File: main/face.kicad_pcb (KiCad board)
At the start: 2 copper layers, 100 x 100 mm, 114 parts

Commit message: added front face, moved around minute mark LEDs so they were spaced evenly and as close together as possible without interfering with USB
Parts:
- removed H1, H2, H3, H4: MountingHole, MountingHole:MountingHole_2.1mm
- added REF**: TestPoint_Pad_D4.0mm, TestPoint:TestPoint_Pad_D4.0mm, B.Cu at (7.81, 22.4)
- added REF**: TestPoint_Pad_D4.0mm, TestPoint:TestPoint_Pad_D4.0mm, B.Cu at (95.0, 5.00)
- added REF**: TestPoint_Pad_D4.0mm, TestPoint:TestPoint_Pad_D4.0mm, B.Cu at (95.0, 95.0)
- added REF**: TestPoint_Pad_D4.0mm, TestPoint:TestPoint_Pad_D4.0mm, B.Cu at (5.00, 95.0)
- added REF**: minute_hole, william_fab:minute_hole, F.Cu at (76.0, 92.6)
- added REF**: minute_hole, william_fab:minute_hole, F.Cu at (58.7, 92.6)
- added REF**: minute_hole, william_fab:minute_hole, F.Cu at (41.3, 92.6)
- added REF**: minute_hole, william_fab:minute_hole, F.Cu at (24.0, 92.6)
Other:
- board text added: "ABCDEFGHIJKL"
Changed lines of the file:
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@@
   (general
     (thickness 1.6)
-    (drawings 9)
+    (drawings 10)
     (tracks 0)
     (zones 0)
-    (modules 114)
+    (modules 118)
     (nets 1)
   )
@@
     (mod_text_size 0.6 0.6)
     (mod_text_width 0.13)
-    (pad_size 6 6)
-    (pad_drill 3)
+    (pad_size 4 4)
+    (pad_drill 0)
     (pad_to_mask_clearance 0.051)
     (solder_mask_min_width 0.25)
@@
     (uvia_drill 0.1)
   )
+  (module TestPoint:TestPoint_Pad_D4.0mm (layer B.Cu)
+    (at 7.814 22.414)
+    (descr "SMD pad as test Point, diameter 4.0mm")
+    (tags "test point SMD pad")
+    (attr virtual)
+    (fp_text reference REF** (at 0 2.898) (layer B.SilkS)
+      (effects (font (size 1 1) (thickness 0.15)) (justify mirror))
+    )
+    (fp_text value TestPoint_Pad_D4.0mm (at 0 -3.1) (layer B.Fab)
+      (effects (font (size 1 1) (thickness 0.15)) (justify mirror))
+    )
+    (fp_text user %R (at 0 2.9) (layer B.Fab)
+      (effects (font (size 1 1) (thickness 0.15)) (justify mirror))
+    )
+    (fp_circle (center 0 0) (end 2.5 0) (layer B.CrtYd) (width 0.05))
+    (fp_circle (center 0 0) (end 0 -2.25) (layer B.SilkS) (width 0.12))
+    (pad 1 smd circle (at 0 0) (size 4 4) (layers B.Cu B.Mask))
+  )
+  (module TestPoint:TestPoint_Pad_D4.0mm (layer B.Cu)
+    (at 95 5)
+    (descr "SMD pad as test Point, diameter 4.0mm")
+    (tags "test point SMD pad")
+    (attr virtual)
+    (fp_text reference REF** (at 0 2.898) (layer B.SilkS)
+      (effects (font (size 1 1) (thickness 0.15)) (justify mirror))
+    )
+    (fp_text value TestPoint_Pad_D4.0mm (at 0 -3.1) (layer B.Fab)
+      (effects (font (size 1 1) (thickness 0.15)) (justify mirror))
+    )
+    (fp_circle (center 0 0) (end 0 -2.25) (layer B.SilkS) (width 0.12))
+    (fp_circle (center 0 0) (end 2.5 0) (layer B.CrtYd) (width 0.05))
+    (fp_text user %R (at 0 2.9) (layer B.Fab)
+      (effects (font (size 1 1) (thickness 0.15)) (justify mirror))
+    )
+    (pad 1 smd circle (at 0 0) (size 4 4) (layers B.Cu B.Mask))
+  )
+  (module TestPoint:TestPoint_Pad_D4.0mm (layer B.Cu)
+    (at 95 95)
+    (descr "SMD pad as test Point, diameter 4.0mm")
+    (tags "test point SMD pad")
+    (attr virtual)
+    (fp_text reference REF** (at 0 2.898) (layer B.SilkS)
+      (effects (font (size 1 1) (thickness 0.15)) (justify mirror))
+    )
+    (fp_text value TestPoint_Pad_D4.0mm (at 0 -3.1) (layer B.Fab)
+      (effects (font (size 1 1) (thickness 0.15)) (justify mirror))
+    )
+    (fp_text user %R (at 0 2.9) (layer B.Fab)
+      (effects (font (size 1 1) (thickness 0.15)) (justify mirror))
+    )
+    (fp_circle (center 0 0) (end 2.5 0) (layer B.CrtYd) (width 0.05))
+    (fp_circle (center 0 0) (end 0 -2.25) (layer B.SilkS) (width 0.12))
+    (pad 1 smd circle (at 0 0) (size 4 4) (layers B.Cu B.Mask))
+  )
+  (module TestPoint:TestPoint_Pad_D4.0mm (layer B.Cu)
+    (at 5 95)
+    (descr "SMD pad as test Point, diameter 4.0mm")
+    (tags "test point SMD pad")
+    (attr virtual)
+    (fp_text reference REF** (at 0 2.898) (layer B.SilkS)
+      (effects (font (size 1 1) (thickness 0.15)) (justify mirror))
+    )
+    (fp_text value TestPoint_Pad_D4.0mm (at 0 -3.1) (layer B.Fab)
+      (effects (font (size 1 1) (thickness 0.15)) (justify mirror))
+    )
+    (fp_circle (center 0 0) (end 0 -2.25) (layer B.SilkS) (width 0.12))
+    (fp_circle (center 0 0) (end 2.5 0) (layer B.CrtYd) (width 0.05))
+    (fp_text user %R (at 0 2.9) (layer B.Fab)
+      (effects (font (size 1 1) (thickness 0.15)) (justify mirror))
+    )
+    (pad 1 smd circle (at 0 0) (size 4 4) (layers B.Cu B.Mask))
+  )
+  (module william_fab:minute_hole (layer F.Cu)
+    (at 76 92.645)
+    (fp_text reference REF** (at -0.1 4.5) (layer F.SilkS) hide
+      (effects (font (size 1 1) (thickness 0.15)))
+    )
+    (fp_text value minute_hole (at -0.05 -5.4) (layer F.Fab)
+      (effects (font (size 1 1) (thickness 0.15)))
+    )
+    (fp_circle (center 0 0) (end 0.001 0) (layer F.Mask) (width 3))
+    (fp_circle (center 0 0) (end 0.001 0) (layer B.Mask) (width 4))
+  )
+  (module william_fab:minute_hole (layer F.Cu)
+    (at 58.666666 92.645)
+    (fp_text reference REF** (at -0.1 4.5) (layer F.SilkS) hide
+      (effects (font (size 1 1) (thickness 0.15)))
+    )
+    (fp_text value minute_hole (at -0.05 -5.4) (layer F.Fab)
+      (effects (font (size 1 1) (thickness 0.15)))
+    )
+    (fp_circle (center 0 0) (end 0.001 0) (layer F.Mask) (width 3))
+    (fp_circle (center 0 0) (end 0.001 0) (layer B.Mask) (width 4))
+  )
+  (module william_fab:minute_hole (layer F.Cu)
+    (at 41.3333 92.645)
+    (fp_text reference REF** (at -0.1 4.5) (layer F.SilkS) hide
+      (effects (font (size 1 1) (thickness 0.15)))
+    )
+    (fp_text value minute_hole (at -0.05 -5.4) (layer F.Fab)
+      (effects (font (size 1 1) (thickness 0.15)))
+    )
+    (fp_circle (center 0 0) (end 0.001 0) (layer F.Mask) (width 3))
+    (fp_circle (center 0 0) (end 0.001 0) (layer B.Mask) (width 4))
+  )
+  (module william_fab:minute_hole (layer F.Cu)
+    (at 24 92.645)
+    (fp_text reference REF** (at -0.1 4.5) (layer F.SilkS) hide
+      (effects (font (size 1 1) (thickness 0.15)))
+    )
+    (fp_text value minute_hole (at -0.05 -5.4) (layer F.Fab)
+      (effects (font (size 1 1) (thickness 0.15)))
+    )
+    (fp_circle (center 0 0) (end 0.001 0) (layer F.Mask) (width 3))
+    (fp_circle (center 0 0) (end 0.001 0) (layer B.Mask) (width 4))
+  )
   (module william_fab:ws2812b-mini_hole (layer F.Cu)
     (at 84.2172 84.39)
@@
     (pad 1 thru_hole circle (at 0 0) (size 6.1 6.1) (drill 6) (layers *.Cu *.Mask))
   )
-  (module MountingHole:MountingHole_2.1mm (layer F.Cu)
-    (at 95 5)
-    (descr "Mounting Hole 2.1mm, no annular")
-    (tags "mounting hole 2.1mm no annular")
-    (attr virtual)
-    (fp_text reference H4 (at 0 -3.2) (layer F.SilkS)
-      (effects (font (size 0.6 0.6) (thickness 0.13)))
-    )
-    (fp_text value MountingHole (at 0 3.2) (layer F.Fab)
-      (effects (font (size 1 1) (thickness 0.15)))
-    )
-    (fp_circle (center 0 0) (end 2.35 0) (layer F.CrtYd) (width 0.05))
-    (fp_circle (center 0 0) (end 2.1 0) (layer Cmts.User) (width 0.15))
-    (fp_text user %R (at 0.3 0) (layer F.Fab)
-      (effects (font (size 0.6 0.6) (thickness 0.13)))
-    )
-    (pad "" np_thru_hole circle (at 0 0) (size 2.1 2.1) (drill 2.1) (layers *.Cu *.Mask))
-  )
-  (module MountingHole:MountingHole_2.1mm (layer F.Cu)
-    (at 95 95)
-    (descr "Mounting Hole 2.1mm, no annular")
-    (tags "mounting hole 2.1mm no annular")
-    (attr virtual)
-    (fp_text reference H3 (at 0 -3.2) (layer F.SilkS)
-      (effects (font (size 0.6 0.6) (thickness 0.13)))
-    )
-    (fp_text value MountingHole (at 0 3.2) (layer F.Fab)
-      (effects (font (size 1 1) (thickness 0.15)))
-    )
-    (fp_circle (center 0 0) (end 2.35 0) (layer F.CrtYd) (width 0.05))
-    (fp_circle (center 0 0) (end 2.1 0) (layer Cmts.User) (width 0.15))
-    (fp_text user %R (at 0.3 0) (layer F.Fab)
-      (effects (font (size 0.6 0.6) (thickness 0.13)))
-    )
-    (pad "" np_thru_hole circle (at 0 0) (size 2.1 2.1) (drill 2.1) (layers *.Cu *.Mask))
-  )
-  (module MountingHole:MountingHole_2.1mm (layer F.Cu)
-    (at 5 95)
-    (descr "Mounting Hole 2.1mm, no annular")
-    (tags "mounting hole 2.1mm no annular")
-    (attr virtual)
-    (fp_text reference H2 (at 0 -3.2) (layer F.SilkS)
-      (effects (font (size 0.6 0.6) (thickness 0.13)))
-    )
-    (fp_text value MountingHole (at 0 3.2) (layer F.Fab)
-      (effects (font (size 1 1) (thickness 0.15)))
-    )
-    (fp_circle (center 0 0) (end 2.35 0) (layer F.CrtYd) (width 0.05))
-    (fp_circle (center 0 0) (end 2.1 0) (layer Cmts.User) (width 0.15))
-    (fp_text user %R (at 0.3 0) (layer F.Fab)
-      (effects (font (size 0.6 0.6) (thickness 0.13)))
-    )
-    (pad "" np_thru_hole circle (at 0 0) (size 2.1 2.1) (drill 2.1) (layers *.Cu *.Mask))
-  )
-  (module MountingHole:MountingHole_2.1mm (layer F.Cu)
-    (at 7.814 22.414)
-    (descr "Mounting Hole 2.1mm, no annular")
-    (tags "mounting hole 2.1mm no annular")
-    (attr virtual)
-    (fp_text reference H1 (at 3.4 0) (layer F.SilkS)
-      (effects (font (size 0.6 0.6) (thickness 0.13)))
-    )
-    (fp_text value MountingHole (at 0 3.2) (layer F.Fab)
-      (effects (font (size 1 1) (thickness 0.15)))
-    )
-    (fp_circle (center 0 0) (end 2.35 0) (layer F.CrtYd) (width 0.05))
-    (fp_circle (center 0 0) (end 2.1 0) (layer Cmts.User) (width 0.15))
-    (fp_text user %R (at 0.3 0) (layer F.Fab)
-      (effects (font (size 0.6 0.6) (thickness 0.13)))
-    )
-    (pad "" np_thru_hole circle (at 0 0) (size 2.1 2.1) (drill 2.1) (layers *.Cu *.Mask))
+  (gr_text ABCDEFGHIJKL (at 42.2056 6.412) (layer F.Mask)
+    (effects (font (size 5 5) (thickness 0.8)))
   )
   (dimension 7.62 (width 0.13) (layer Cmts.User)

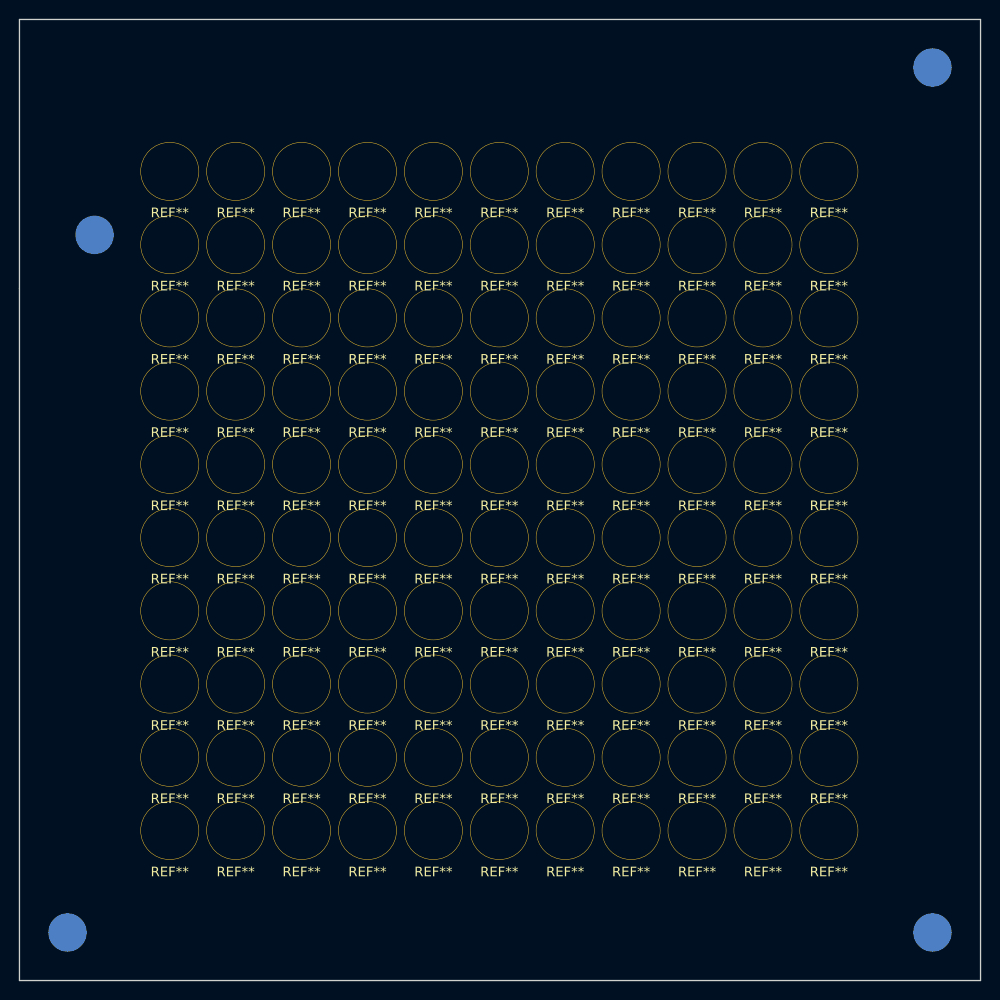
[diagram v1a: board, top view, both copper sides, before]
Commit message: progress and yet not.  trying for v0.2.0, but some issues: letters not aligned, switches to tall, minute leds too close to USB_C
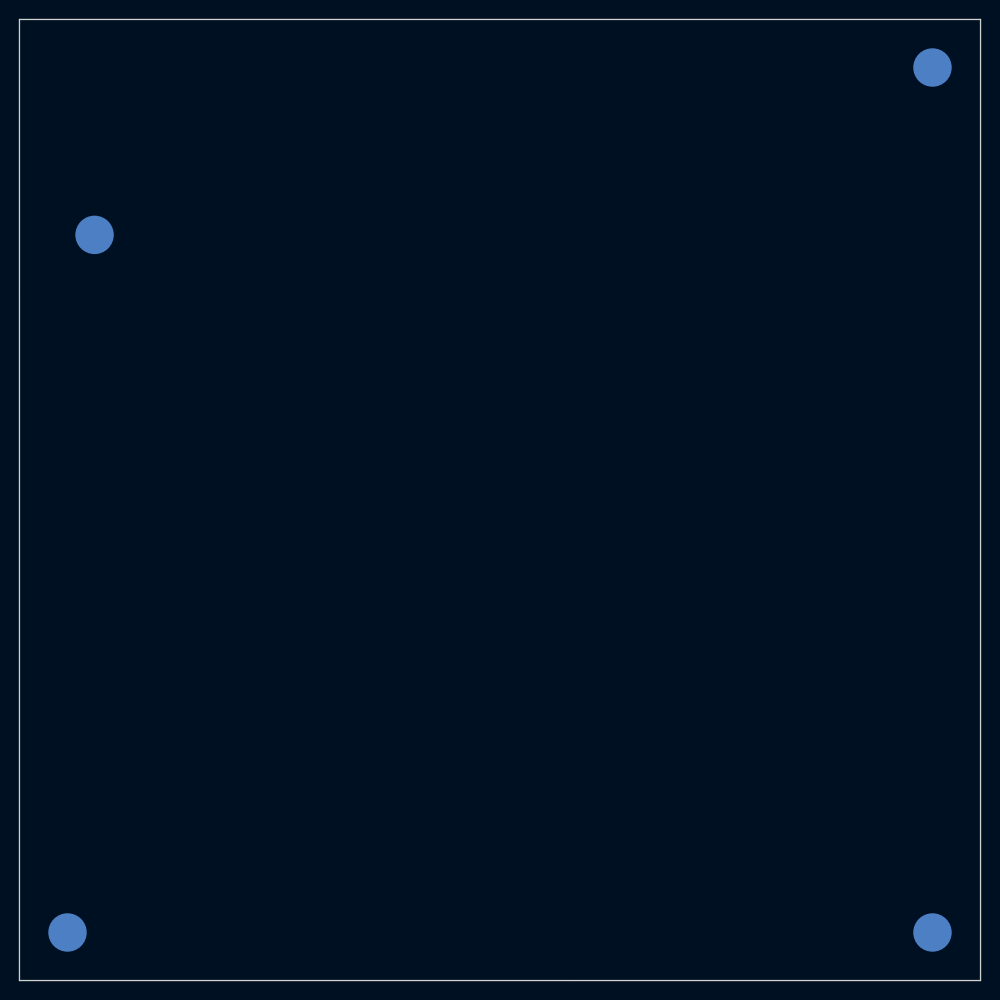
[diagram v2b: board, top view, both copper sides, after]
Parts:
- removed the REF** at (77.4, 84.4)
- removed the REF** at (63.6, 23.4)
- removed the REF** at (56.8, 23.4)
- removed the REF** at (49.9, 23.4)
- removed the REF** at (43.1, 23.4)
- removed the REF** at (36.2, 23.4)
- removed the REF** at (29.4, 23.4)
- removed the REF** at (22.5, 23.4)
- removed the REF** at (15.6, 23.4)
- removed the REF** at (84.2, 15.8)
- removed the REF** at (77.4, 15.8)
- removed the REF** at (70.5, 84.4)
- removed the REF** at (70.5, 15.8)
- removed the REF** at (63.6, 15.8)
- removed the REF** at (56.8, 15.8)
- removed the REF** at (49.9, 15.8)
- removed the REF** at (43.1, 15.8)
- removed the REF** at (36.2, 15.8)
- removed the REF** at (29.4, 15.8)
- removed the REF** at (22.5, 15.8)
- removed the REF** at (15.6, 15.8)
- removed the REF** at (63.6, 84.4)
- removed the REF** at (56.8, 84.4)
- removed the REF** at (49.9, 84.4)
- removed the REF** at (43.1, 84.4)
- removed the REF** at (36.2, 84.4)
- removed the REF** at (29.4, 84.4)
- removed the REF** at (22.5, 84.4)
- removed the REF** at (15.6, 84.4)
- removed the REF** at (84.2, 76.8)
- removed the REF** at (77.4, 76.8)
- removed the REF** at (70.5, 76.8)
- removed the REF** at (63.6, 76.8)
- removed the REF** at (56.8, 76.8)
- removed the REF** at (49.9, 76.8)
- removed the REF** at (43.1, 76.8)
- removed the REF** at (36.2, 76.8)
- removed the REF** at (29.4, 76.8)
- removed the REF** at (22.5, 76.8)
- removed the REF** at (15.6, 76.8)
- removed the REF** at (84.2, 69.2)
- removed the REF** at (77.4, 69.2)
- removed the REF** at (70.5, 69.2)
- removed the REF** at (63.6, 69.2)
- removed the REF** at (56.8, 69.2)
- removed the REF** at (49.9, 69.2)
- removed the REF** at (43.1, 69.2)
- removed the REF** at (36.2, 69.2)
- removed the REF** at (29.4, 69.2)
- removed the REF** at (22.5, 69.2)
- removed the REF** at (15.6, 69.2)
- removed the REF** at (84.2, 61.5)
- removed the REF** at (77.4, 61.5)
- removed the REF** at (70.5, 61.5)
- removed the REF** at (63.6, 61.5)
- removed the REF** at (56.8, 61.5)
- removed the REF** at (49.9, 61.5)
- removed the REF** at (43.1, 61.5)
- removed the REF** at (36.2, 61.5)
- removed the REF** at (29.4, 61.5)
- removed the REF** at (22.5, 61.5)
- removed the REF** at (15.6, 61.5)
- removed the REF** at (84.2, 53.9)
- removed the REF** at (77.4, 53.9)
- removed the REF** at (70.5, 53.9)
- removed the REF** at (63.6, 53.9)
- removed the REF** at (56.8, 53.9)
- removed the REF** at (49.9, 53.9)
- removed the REF** at (43.1, 53.9)
- removed the REF** at (36.2, 53.9)
- removed the REF** at (29.4, 53.9)
- removed the REF** at (22.5, 53.9)
- removed the REF** at (15.6, 53.9)
- removed the REF** at (84.2, 46.3)
- removed the REF** at (77.4, 46.3)
- removed the REF** at (70.5, 46.3)
- removed the REF** at (63.6, 46.3)
- removed the REF** at (56.8, 46.3)
- removed the REF** at (49.9, 46.3)
- removed the REF** at (43.1, 46.3)
- removed the REF** at (36.2, 46.3)
- removed the REF** at (29.4, 46.3)
- removed the REF** at (22.5, 46.3)
- removed the REF** at (15.6, 46.3)
- removed the REF** at (84.2, 38.7)
- removed the REF** at (77.4, 38.7)
- removed the REF** at (70.5, 38.7)
- removed the REF** at (63.6, 38.7)
- removed the REF** at (56.8, 38.7)
- removed the REF** at (49.9, 38.7)
- removed the REF** at (43.1, 38.7)
- removed the REF** at (36.2, 38.7)
- removed the REF** at (29.4, 38.7)
- removed the REF** at (22.5, 38.7)
- removed the REF** at (15.6, 38.7)
- removed the REF** at (84.2, 31.1)
- removed the REF** at (77.4, 31.1)
- removed the REF** at (70.5, 31.1)
- removed the REF** at (63.6, 31.1)
- removed the REF** at (84.2, 84.4)
- removed the REF** at (56.8, 31.1)
- removed the REF** at (49.9, 31.1)
- removed the REF** at (43.1, 31.1)
- removed the REF** at (36.2, 31.1)
- removed the REF** at (29.4, 31.1)
- removed the REF** at (22.5, 31.1)
- removed the REF** at (15.6, 31.1)
- removed the REF** at (84.2, 23.4)
- removed the REF** at (77.4, 23.4)
- removed the REF** at (70.5, 23.4)
- added G***: LOGO, graphics:face, F.Cu at (50.0, 50.0)
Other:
- board text removed: "ABCDEFGHIJKL"
